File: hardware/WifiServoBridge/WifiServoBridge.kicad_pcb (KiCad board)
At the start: 2 copper layers, 67.3 x 58.4 mm, 19 parts, among them J1 Conn_01x02, J10 Conn_01x03, J2 Conn_01x02, J3 Conn_01x19, J4 Conn_01x19, J5 Conn_01x03, J6 Conn_01x03, J7 Conn_01x03, J8 Conn_01x03, J9 Conn_01x03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

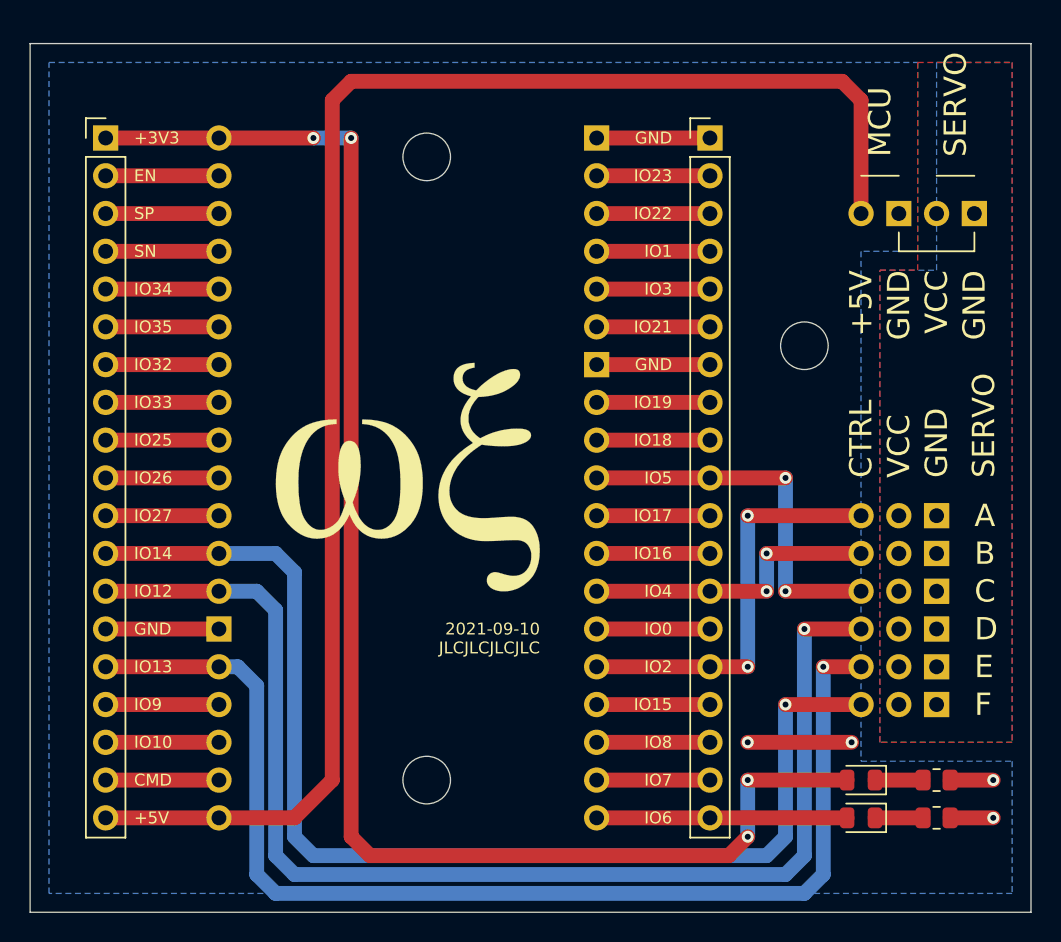
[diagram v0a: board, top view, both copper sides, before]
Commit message: Simplified PWM routing
Used the physically closed PWM capable pins.
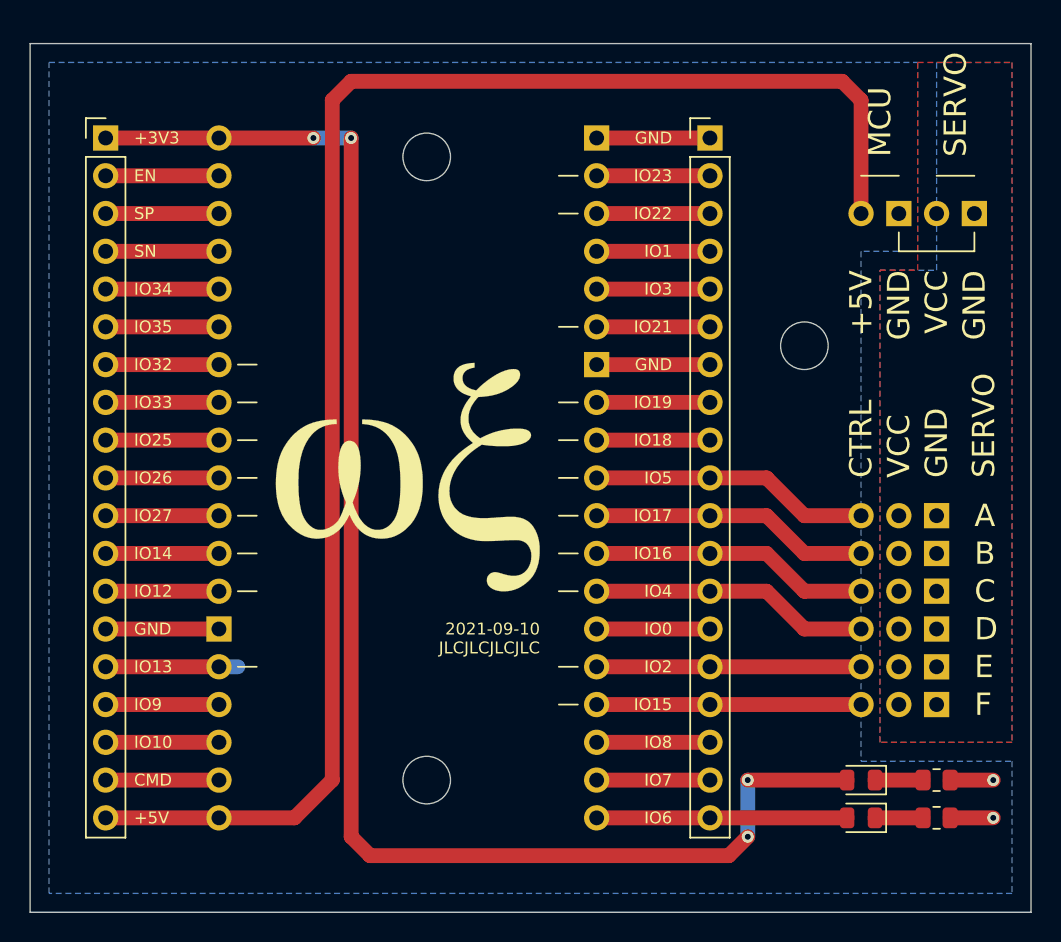
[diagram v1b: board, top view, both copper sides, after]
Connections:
- J10 pad 1: SERVO_F -> MCU_GPIO15
- J3 pad 12: SERVO_F -> MCU_GPIO14
- J3 pad 13: SERVO_D -> MCU_GPIO12
- J3 pad 15: SERVO_E -> MCU_GPIO13
- J4 pad 10: SERVO_C -> MCU_GPIO5
- J4 pad 13: SERVO_B -> MCU_GPIO4
- J4 pad 15: SERVO_A -> MCU_GPIO2
- J5 pad 1: SERVO_A -> MCU_GPIO5
- J6 pad 1: SERVO_B -> MCU_GPIO17
- J7 pad 1: SERVO_C -> MCU_GPIO16
- J8 pad 1: SERVO_D -> MCU_GPIO4
- J9 pad 1: SERVO_E -> MCU_GPIO2
- U1 pad 10: SERVO_A -> MCU_GPIO2
- U1 pad 12: SERVO_B -> MCU_GPIO4
- U1 pad 13: SERVO_C -> MCU_GPIO5
- U1 pad 19: SERVO_D -> MCU_GPIO12
- U1 pad 20: SERVO_E -> MCU_GPIO13
- U1 pad 21: SERVO_F -> MCU_GPIO14
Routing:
- net SERVO_D: track 84.1 -> 0.00 mm, vias 1 -> 0
- net SERVO_F: track 79.0 -> 0.00 mm, vias 1 -> 0
- net SERVO_E: track 79.0 -> 0.00 mm, vias 1 -> 0
- net SERVO_A: track 27.9 -> 0.00 mm, vias 2 -> 0
- net SERVO_C: track 25.4 -> 0.00 mm, vias 2 -> 0
- net SERVO_B: track 20.3 -> 0.00 mm, vias 2 -> 0
- net MCU_GPIO5: track 0.00 -> 18.8 mm
- net MCU_GPIO4: track 0.00 -> 18.8 mm
- net MCU_GPIO2: track 0.00 -> 17.8 mm
- net MCU_GPIO17: track 7.62 -> 18.8 mm
- net MCU_GPIO16: track 7.62 -> 18.8 mm
- net MCU_GPIO15: track 7.62 -> 17.8 mm
- net MCU_GPIO13: track 0.00 -> 8.89 mm
- net MCU_GPIO14: track 0.00 -> 7.62 mm
- net MCU_GPIO12: track 0.00 -> 7.62 mm
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
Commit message: Add VCC LED and silkscreen labels
Closes issue #1 and issue #2
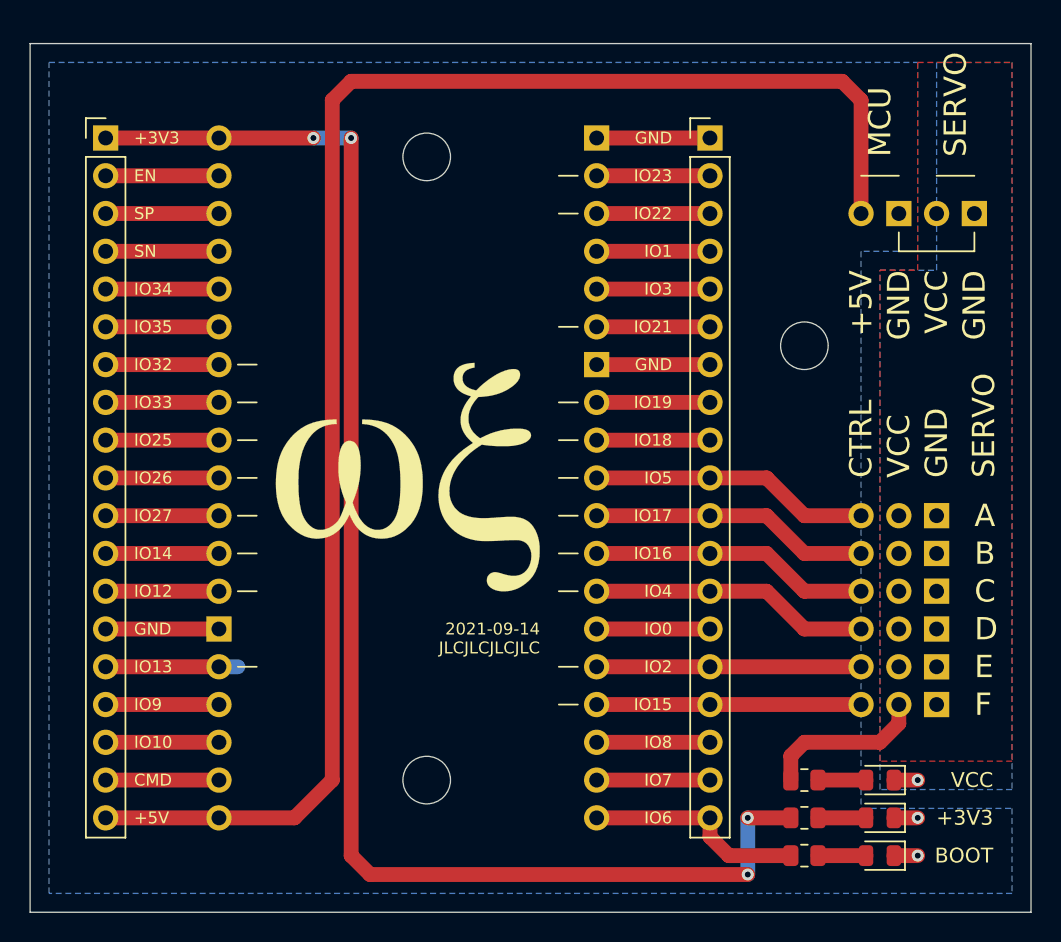
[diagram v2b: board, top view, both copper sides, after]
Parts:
- added D1: VCC, LED_SMD:LED_0805_2012Metric, F.Cu at (403.9, -86.4)
- added R2: 660 Ω, Resistor_SMD:R_0805_2012Metric, F.Cu at (398.8, -83.8)
- D2: renamed from D1; value PWR -> MCU
- R1: value 660 Ω -> 1000 Ω
- moved R3 9.25 mm to (398.8, -81.3)
- moved R1 8.89 mm to (398.8, -86.4)
- moved D2 2.84 mm to (403.9, -83.8)
- moved D3 2.84 mm to (403.9, -81.3)
- renumbered D2 to D3, R2 to R3
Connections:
- D2 pad 1: Net-(D1-Pad1) -> MCU_GND
- D2 pad 2: MCU_+3V3 -> Net-(D2-Pad2)
- D3 pad 1: Net-(D2-Pad1) -> MCU_GND
- D3 pad 2: DEBUG_LED -> Net-(D3-Pad2)
- R1 pad 1: MCU_GND -> Net-(D1-Pad2)
- R1 pad 2: Net-(D1-Pad1) -> SERVO_VCC
- R3 pad 1: MCU_GND -> Net-(D3-Pad2)
- R3 pad 2: Net-(D2-Pad1) -> DEBUG_LED
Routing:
- net SERVO_VCC: track 0.00 -> 11.1 mm
- net Net-(D3-Pad2): track 0.00 -> 3.23 mm
- net Net-(D2-Pad2): track 0.00 -> 3.23 mm
- net Net-(D2-Pad1): track 3.23 -> 0.00 mm
- net Net-(D1-Pad2): track 0.00 -> 3.23 mm
- net Net-(D1-Pad1): track 3.23 -> 0.00 mm
- net MCU_+3V3: track 101.7 -> 98.7 mm
- net MCU_GND: track 28.7 -> 26.1 mm
- net DEBUG_LED: track 16.8 -> 14.9 mm
- net SERVO_GND: track 0.00 -> 1.60 mm, vias 0 -> 1
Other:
- board text added: "2021-09-14"
- board text added: "BOOT"
- board text removed: "2021-09-10"

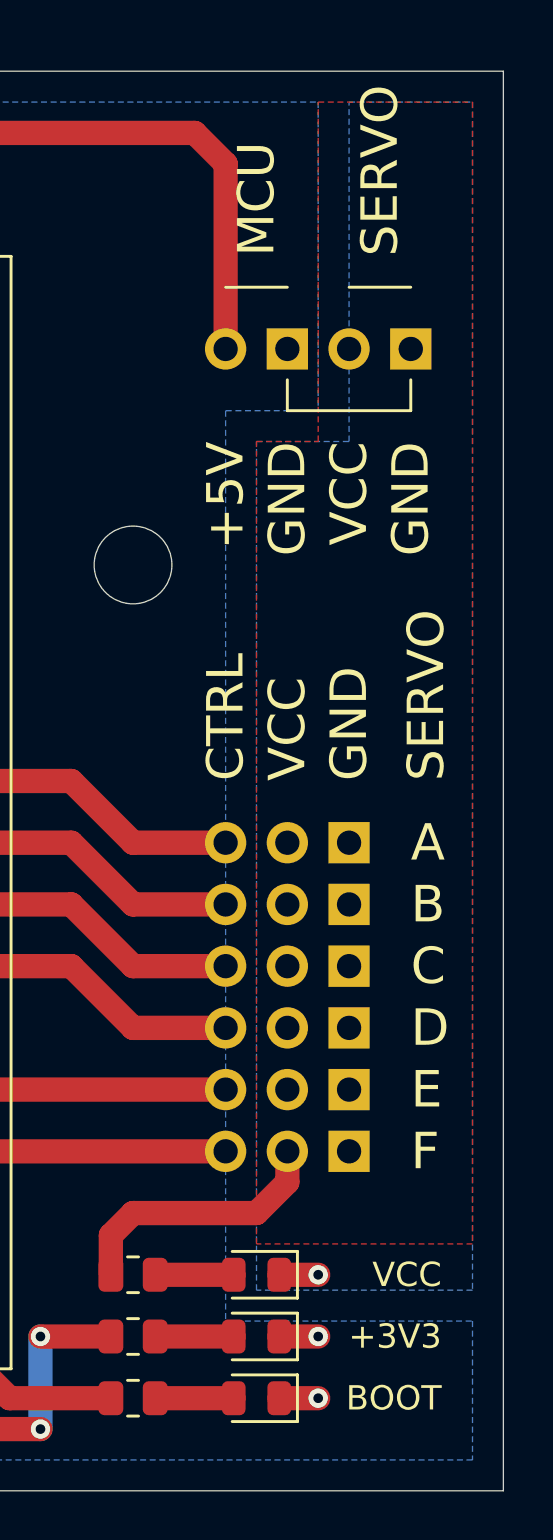
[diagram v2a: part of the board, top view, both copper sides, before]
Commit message: `MCU_GND' and `SERVO_GND' must be connected on board
Since the serve control line is relative to the servo ground potential, MCU and servo ground must be on the same potential.
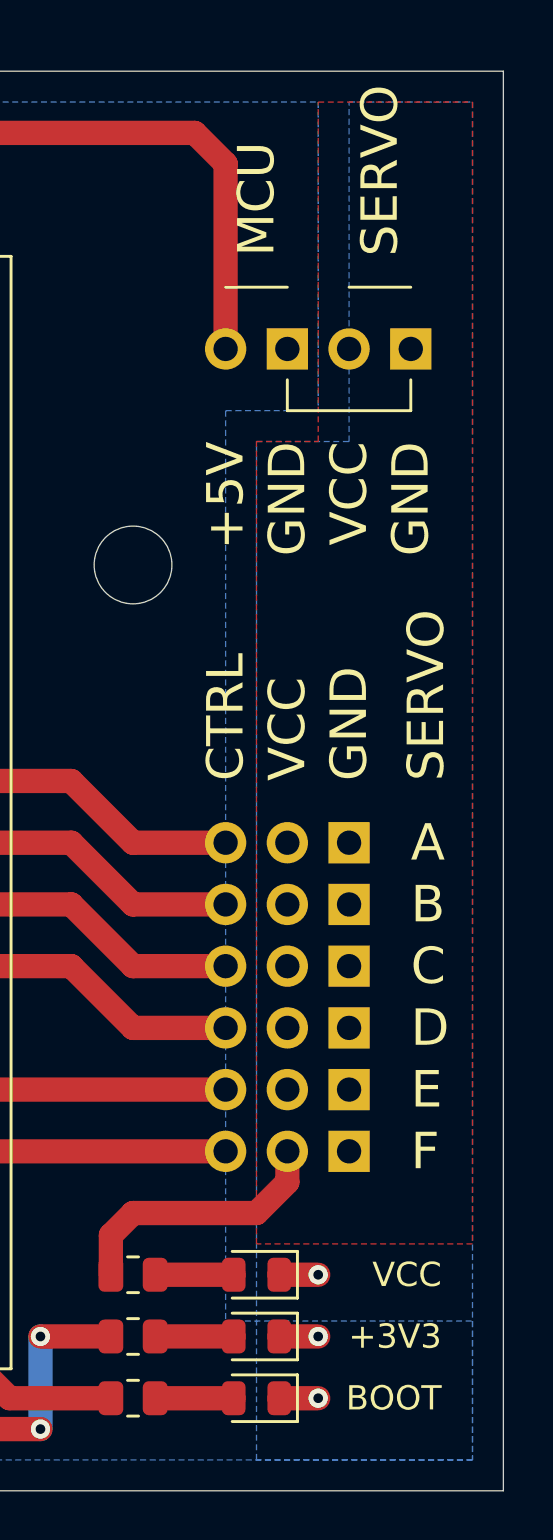
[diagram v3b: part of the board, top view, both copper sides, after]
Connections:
- D1 pad 1: SERVO_GND -> MCU_GND
- J1 pad 2: SERVO_GND -> MCU_GND
- J10 pad 3: SERVO_GND -> MCU_GND
- J5 pad 3: SERVO_GND -> MCU_GND
- J6 pad 3: SERVO_GND -> MCU_GND
- J7 pad 3: SERVO_GND -> MCU_GND
- J8 pad 3: SERVO_GND -> MCU_GND
- J9 pad 3: SERVO_GND -> MCU_GND
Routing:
- net SERVO_GND: track 1.60 -> 0.00 mm, vias 1 -> 0
- net MCU_GND: track 26.1 -> 27.7 mm, vias 2 -> 3
- removed copper zone on B.Cu, net SERVO_GND

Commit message: Improved optics by routing +5V as well as +3V3 on bottom
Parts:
- added REF**: MountingHole_3.2mm_M3, MountingHole:MountingHole_3.2mm_M3, F.Cu at (379.7, -86.4)
- moved REF** 22.2 mm to (379.7, -127.0)
- moved REF** 8.98 mm to (364.5, -127.0)
- moved REF** 8.89 mm to (364.5, -86.4)
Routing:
- net MCU_+5V: track 106.2 -> 123.0 mm, vias 0 -> 1
- net MCU_+3V3: track 98.7 -> 106.1 mm, vias 4 -> 1
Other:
- board text added: "2021-09-15"
- board text removed: "2021-09-14"
